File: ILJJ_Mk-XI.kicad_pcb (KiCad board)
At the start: 2 copper layers, 124.5 x 96.5 mm, 83 parts, among them J0 Conn_02x12_Odd_Even, J1 Conn_02x12_Odd_Even, J2 Conn_02x12_Odd_Even, J3 Conn_02x12_Odd_Even, J4 Conn_02x12_Odd_Even, J5 Conn_02x12_Odd_Even, SW0 SW_Coded_SH-7070, SW1 SW_Coded_SH-7070, SW2 SW_Coded_SH-7070, SW3 SW_Coded_SH-7070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

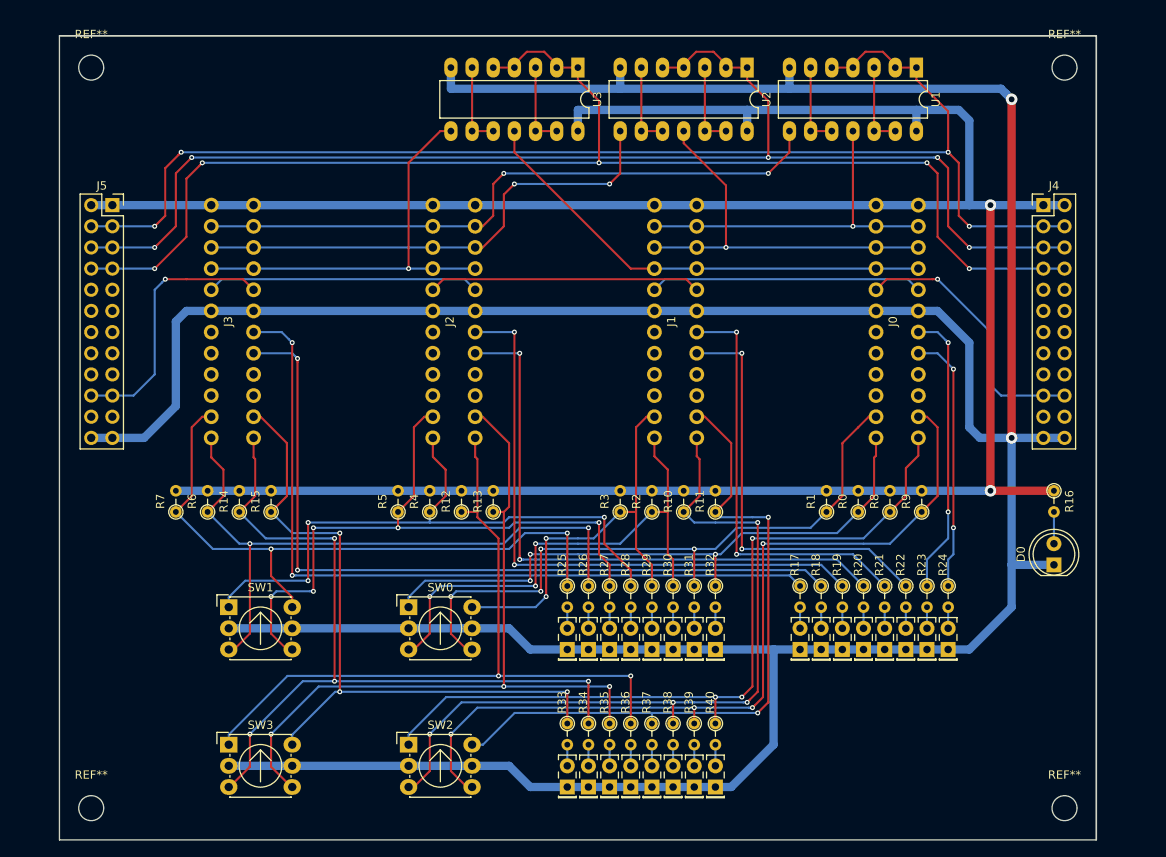
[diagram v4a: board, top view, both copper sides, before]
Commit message: [add] designed in ILJJ logo
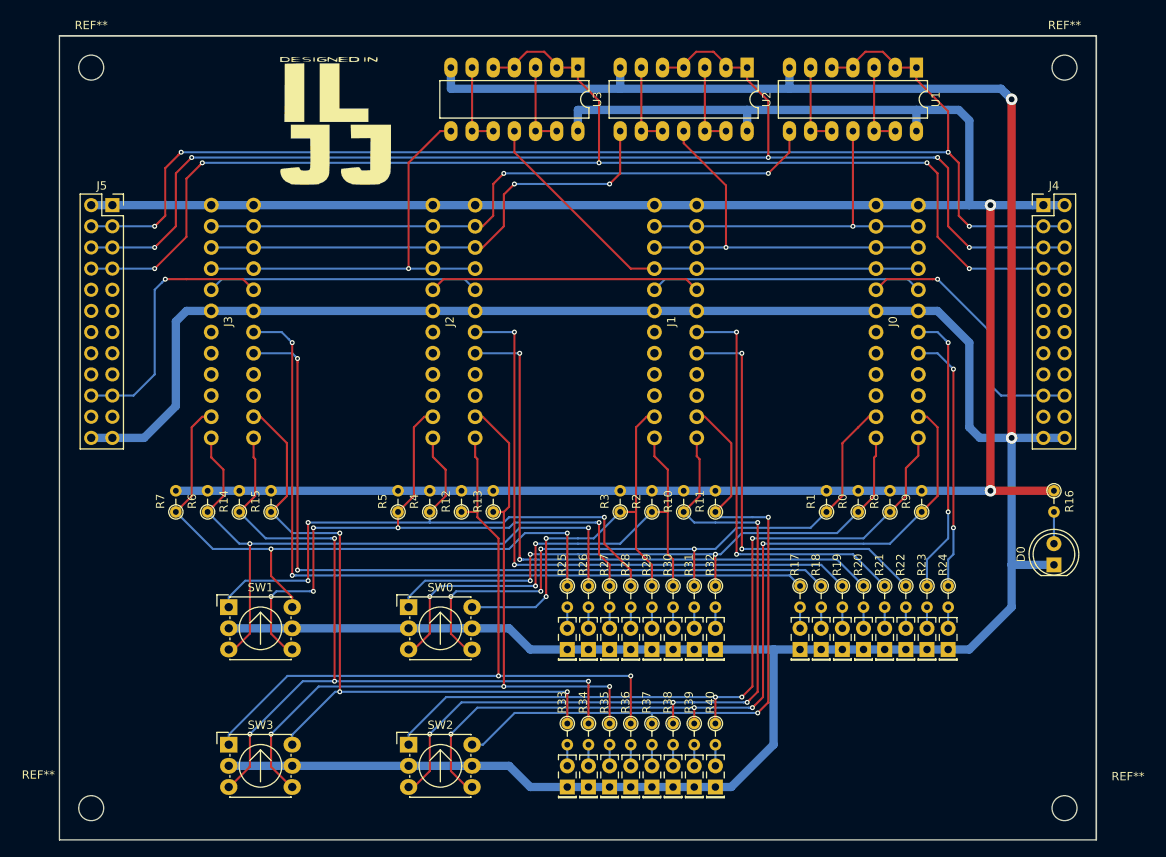
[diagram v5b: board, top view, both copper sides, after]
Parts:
- added G***: LOGO, fplib:designed-in-ILJJ-small, F.Cu at (134.6, 59.7)

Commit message: [clean] ネジ穴のリファレンスを非表示にして角を落とした
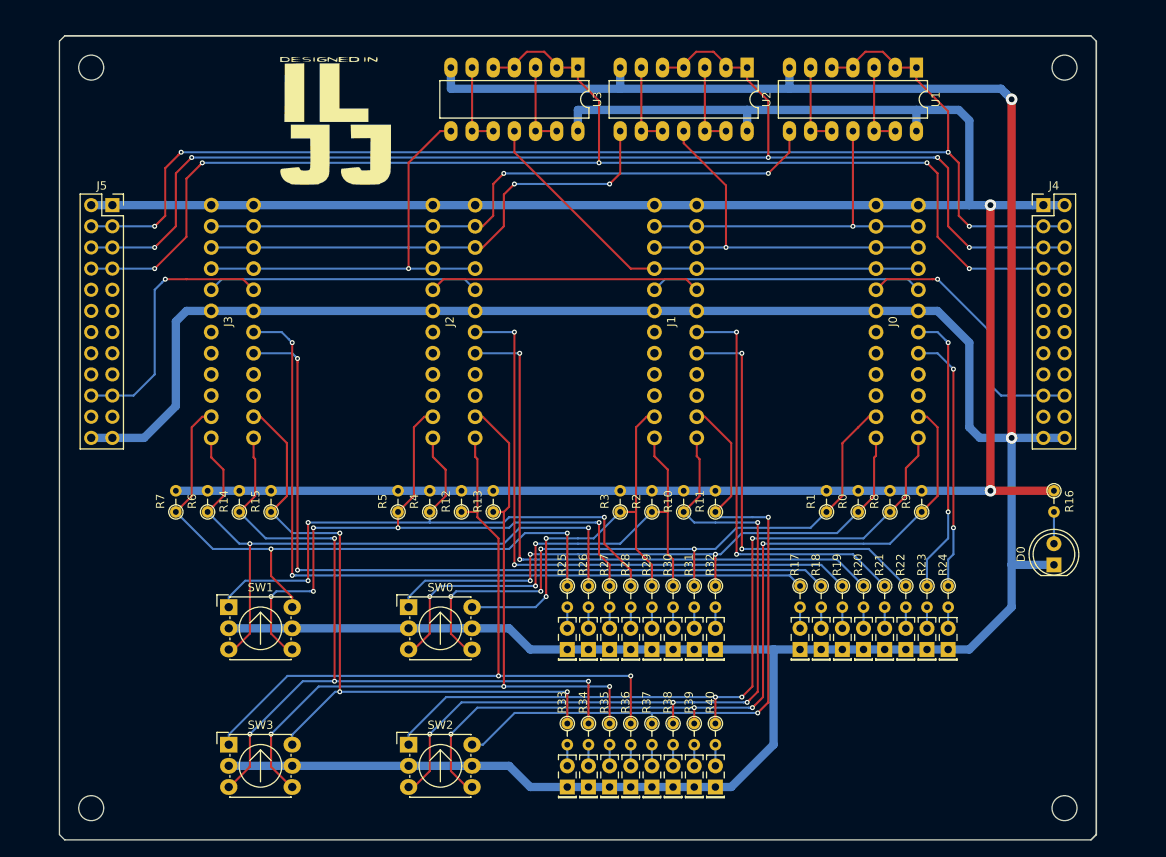
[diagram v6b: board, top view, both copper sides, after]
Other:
- outline, holes or cut-outs redrawn
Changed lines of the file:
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@@
   (general
     (thickness 1.6)
-    (drawings 4)
+    (drawings 8)
     (tracks 622)
     (zones 0)
@@
     (tags "mounting hole 3mm no annular")
     (attr virtual)
-    (fp_text reference REF** (at 0 -5.08) (layer F.SilkS)
+    (fp_text reference REF** (at 0 -5.08) (layer F.SilkS) hide
       (effects (font (size 1 1) (thickness 0.15)))
     )
@@
     (tags "mounting hole 3mm no annular")
     (attr virtual)
-    (fp_text reference REF** (at 7.62 -3.81) (layer F.SilkS)
+    (fp_text reference REF** (at 7.62 -3.81) (layer F.SilkS) hide
       (effects (font (size 1 1) (thickness 0.15)))
     )
@@
     (tags "mounting hole 3mm no annular")
     (attr virtual)
-    (fp_text reference REF** (at -6.35 -4) (layer F.SilkS)
+    (fp_text reference REF** (at -6.35 -4) (layer F.SilkS) hide
       (effects (font (size 1 1) (thickness 0.15)))
     )
@@
     (tags "mounting hole 3mm no annular")
     (attr virtual)
-    (fp_text reference REF** (at 0 -5.08) (layer F.SilkS)
+    (fp_text reference REF** (at 0 -5.08) (layer F.SilkS) hide
       (effects (font (size 1 1) (thickness 0.15)))
     )
@@
       (xy -0.592666 0.508) (xy -0.594526 3.450167)) (layer F.SilkS) (width 0.01))
   )
-  (gr_line (start 101.6 146.05) (end 101.6 49.53) (layer Edge.Cuts) (width 0.15))
-  (gr_line (start 226.06 146.05) (end 101.6 146.05) (layer Edge.Cuts) (width 0.15))
-  (gr_line (start 226.06 49.53) (end 101.6 49.53) (layer Edge.Cuts) (width 0.2))
-  (gr_line (start 226.06 146.05) (end 226.06 49.53) (layer Edge.Cuts) (width 0.2))
+  (gr_line (start 102.235 146.05) (end 101.6 145.415) (layer Edge.Cuts) (width 0.15))
+  (gr_line (start 102.235 49.53) (end 101.6 50.165) (layer Edge.Cuts) (width 0.15))
+  (gr_line (start 225.425 49.53) (end 226.06 50.165) (layer Edge.Cuts) (width 0.15))
+  (gr_line (start 226.06 145.415) (end 225.425 146.05) (layer Edge.Cuts) (width 0.2))
+  (gr_line (start 101.6 145.415) (end 101.6 50.165) (layer Edge.Cuts) (width 0.15))
+  (gr_line (start 225.425 146.05) (end 102.235 146.05) (layer Edge.Cuts) (width 0.15))
+  (gr_line (start 225.425 49.53) (end 102.235 49.53) (layer Edge.Cuts) (width 0.2))
+  (gr_line (start 226.06 145.415) (end 226.06 50.165) (layer Edge.Cuts) (width 0.2))
   (segment (start 220.98 110.49) (end 220.98 106.68) (width 0.25) (layer B.Cu) (net 1) (status 30))
   (segment (start 148.59 55.88) (end 148.59 53.34) (width 1) (layer B.Cu) (net 2) (status 20))
